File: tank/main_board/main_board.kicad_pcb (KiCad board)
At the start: 2 copper layers, 66.5 x 56.2 mm, 41 parts, among them J1 PowerOut, J10 PowerMotor, J11 SigOut, J12 Spk, J14 M0, J15 M1, J16 M2, J2 PowerIn, J3 Encoder0, J4 Encoder1, J5 Encoder2, J6 Encoder3, J7 Bump0, J8 Bump1, J9 Programming Header, U1 L7805, U4 L293D, U5 L293D, Y1 Crystal

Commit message: fixes
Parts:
- removed SN74HC595: SN74HC595, custom:DIP-16_W7.62mm
- added U3: SN74HC595, custom:DIP-16_W7.62mm, F.Cu at (133.6, 103.2)
- renumbered LEDs to J13, ATMEGA328P-PU to U2

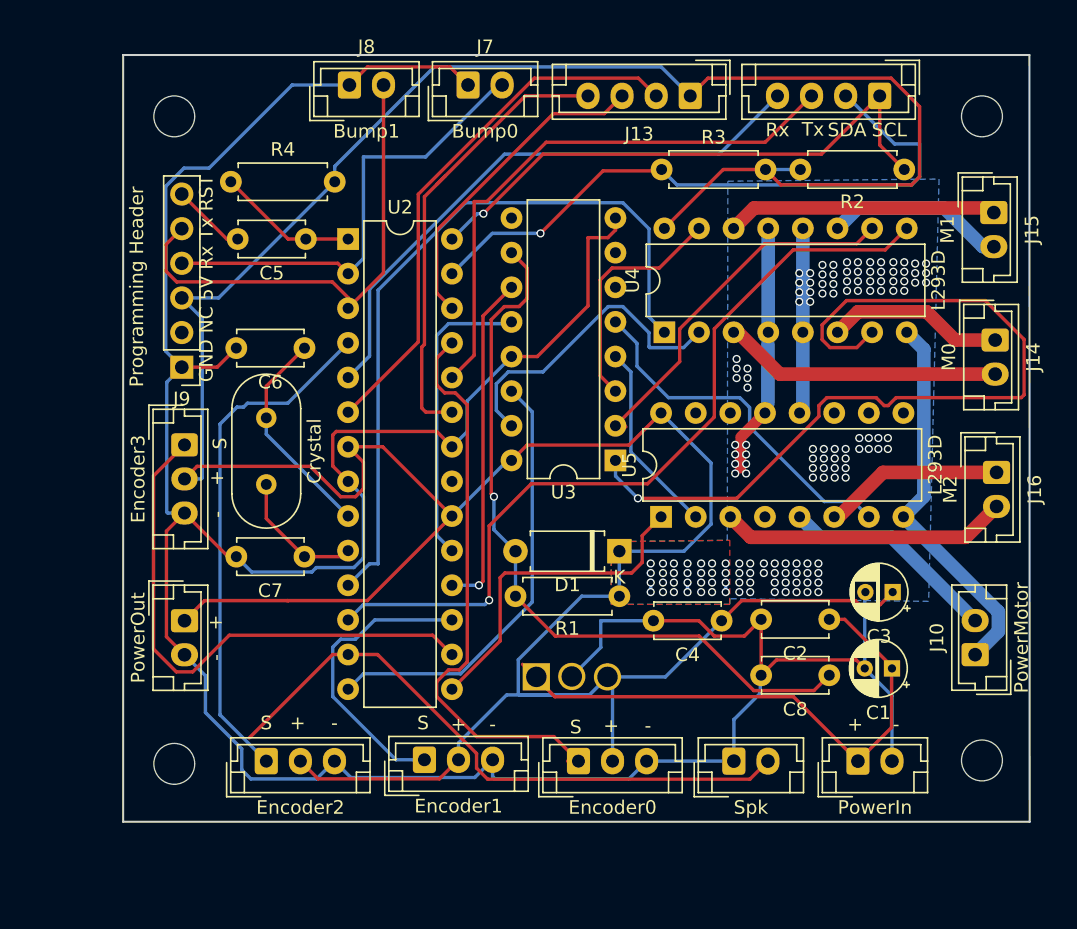
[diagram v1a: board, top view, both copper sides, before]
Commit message: Version 0.11: - Better labelling - Put LED output on Rx and Tx pins. This way, we won't be attaching interrutps to Serial pins
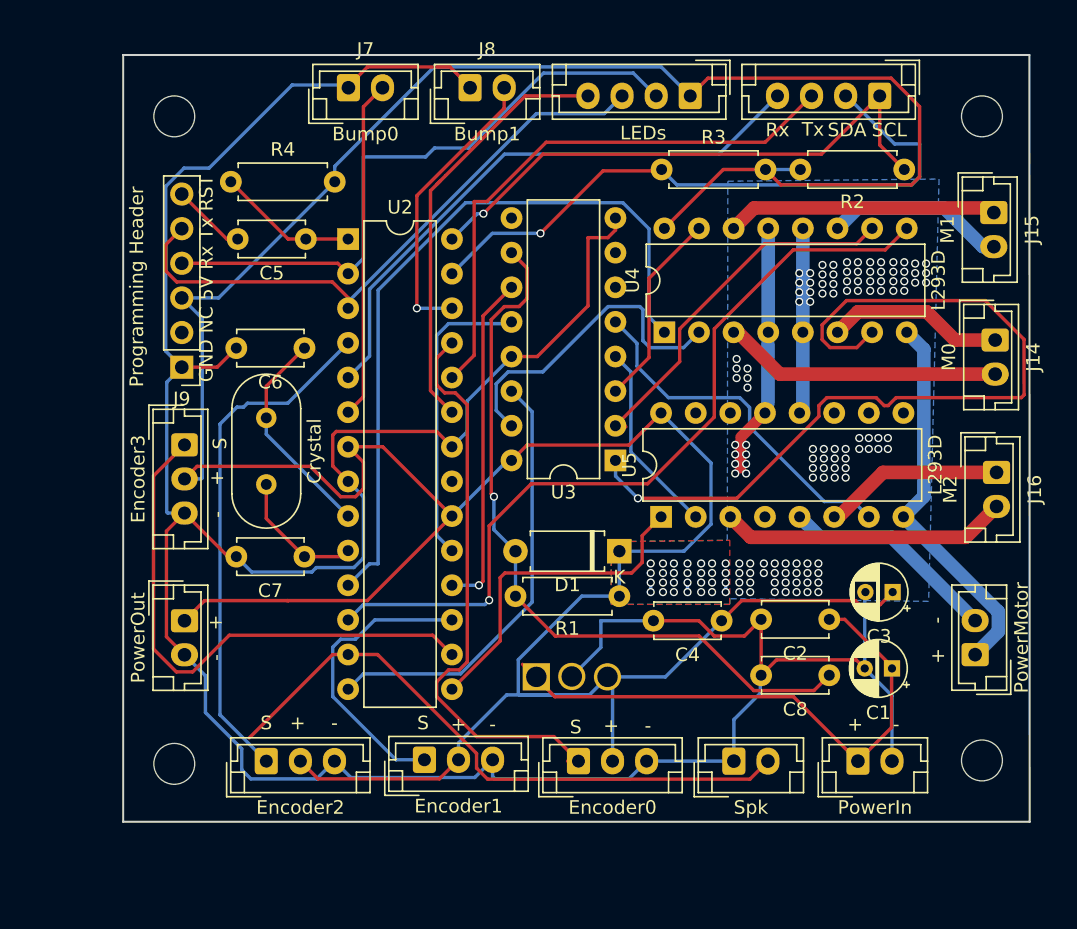
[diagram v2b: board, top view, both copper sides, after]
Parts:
- moved J8 8.85 mm to (123.0, 75.9)
- moved J7 8.78 mm to (114.0, 75.9)
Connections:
- J9 pad 4: Bump0 -> LED0
- J9 pad 5: Bump1 -> LED1
- U2 pad 2: Bump0 -> LED0
- U2 pad 26: LED1 -> Bump1
- U2 pad 3: Bump1 -> LED1
- U2 pad 6: LED0 -> Bump0
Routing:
- net LED1: track 23.9 -> 45.4 mm
- net Bump1: track 36.0 -> 21.7 mm, vias 0 -> 1
- net Bump0: track 33.9 -> 24.8 mm
- net LED0: track 39.6 -> 46.3 mm
- net M1-: track 17.4 -> 14.5 mm
- net LED2: track 33.9 -> 31.7 mm
- net M0+: track 23.4 -> 24.2 mm
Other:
- board text added: "Laser Tag Robot Tank Main Board v0.11 M.I.A.R. Labs nick.groesz@gmail.com"
- board text removed: "Laser Tag Robot Tank Main Board v1.00 M.I.A.R. Labs nick.groesz@gmail.com"

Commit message: debug
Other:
- net class Default removed
- net class Motor removed

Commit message: Main Board v0.12
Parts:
- removed ?: , 
- removed D1: D, custom:D_A-405_P7.62mm_Horizontal
- removed R4: R10, custom:R_Axial_DIN0207_L6.3mm_D2.5mm_P7.62mm_Horizontal
- removed the REF** at (160.5, 125.2)
- removed the REF** at (160.5, 78.0)
- removed the REF** at (101.2, 125.5)
- removed the REF** at (101.2, 78.0)
- added C9: 100nF, custom:C_Disc_D4.7mm_W2.5mm_P5.00mm, F.Cu at (149.0, 104.5)
- added REF**: MountingHole_3mm, custom:MountingHole_3mm, F.Cu at (94.5, 76.5)
- added REF**: MountingHole_3mm, custom:MountingHole_3mm, F.Cu at (159.0, 76.5)
- added REF**: MountingHole_3mm, custom:MountingHole_3mm, F.Cu at (94.0, 130.5)
- added REF**: MountingHole_3mm, custom:MountingHole_3mm, F.Cu at (159.0, 131.0)
- C1: value CP1 -> 10uF
- C2: value C2 -> 100nF
- C3: value CP3 -> 10uF
- C4: value C4 -> 100nF
- C5, C8: value C_Small -> 100nF
- C6: value C6 -> 22pF
- C7: value C7 -> 22pF
- J1: value PowerOut -> Encoder0; footprint custom:JST_EH_B2B-EH-A_1x02_P2.50mm_Vertical -> custom:JST_EH_B3B-EH-A_1x03_P2.50mm_Vertical
- J11: value SigOut -> M0; footprint custom:JST_EH_B4B-EH-A_1x04_P2.50mm_Vertical -> custom:JST_EH_B2B-EH-A_1x02_P2.50mm_Vertical
- J12: value Spk -> M1
- J13: value LEDs -> M2; footprint custom:JST_EH_B4B-EH-A_1x04_P2.50mm_Vertical -> custom:JST_EH_B2B-EH-A_1x02_P2.50mm_Vertical
- J14: value M0 -> Spk
- J15: value M1 -> LEDs; footprint custom:JST_EH_B2B-EH-A_1x02_P2.50mm_Vertical -> custom:JST_EH_B4B-EH-A_1x04_P2.50mm_Vertical
- J16: value M2 -> SigOut; footprint custom:JST_EH_B2B-EH-A_1x02_P2.50mm_Vertical -> custom:JST_EH_B4B-EH-A_1x04_P2.50mm_Vertical
- J2: value PowerIn -> Encoder1; footprint custom:JST_EH_B2B-EH-A_1x02_P2.50mm_Vertical -> custom:JST_EH_B3B-EH-A_1x03_P2.50mm_Vertical
- J3: value Encoder0 -> Encoder2
- J4: value Encoder1 -> Encoder3
- J5: value Encoder2 -> Programming Header; footprint custom:JST_EH_B3B-EH-A_1x03_P2.50mm_Vertical -> custom:PinHeader_1x06_P2.54mm_Vertical
- J6: value Encoder3 -> Bump0; footprint custom:JST_EH_B3B-EH-A_1x03_P2.50mm_Vertical -> custom:JST_EH_B2B-EH-A_1x02_P2.50mm_Vertical
- J7: value Bump0 -> Bump1
- J8: value Bump1 -> PowerOut
- J9: value Programming Header -> PowerIn; footprint custom:PinHeader_1x06_P2.54mm_Vertical -> custom:JST_EH_B2B-EH-A_1x02_P2.50mm_Vertical
- R1: value R -> 10k
- R2: value R7 -> 10k
- R3: value R6 -> 10k
- U1: footprint Custom:L7805CV -> custom:L7805CV
- moved J2 63.5 mm to (95.1, 96.0), turned to -90 degrees
- moved J15 55.5 mm to (129.8, 130.7), turned to 0 degrees
- moved G*** 54.6 mm to (103.6, 81.3)
- moved C2 51.3 mm to (102.5, 94.0), turned to 90 degrees
- moved J13 46.3 mm to (158.5, 118.5), turned to 90 degrees
- moved J16 42.5 mm to (128.5, 77.5), turned to 180 degrees
- moved J14 40.5 mm to (143.5, 130.7), turned to 0 degrees
- moved J3 40.0 mm to (95.1, 107.5), turned to -90 degrees
- moved R1 39.3 mm to (108.8, 83.0)
- moved R2 35.0 mm to (119.8, 83.0)
- moved C4 34.6 mm to (125.0, 84.5), turned to 0 degrees
- moved J9 34.1 mm to (100.5, 130.5), turned to 0 degrees
- moved C1 33.8 mm to (120.5, 123.8), turned to 0 degrees
- moved C3 33.7 mm to (120.6, 117.9), turned to 0 degrees
- moved J1 31.3 mm to (95.1, 84.5)
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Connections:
- C2 pad 1: 9V -> 4.5V
- C8 pad 1: Net-(C8-Pad1) -> GND
- C8 pad 2: GND -> 4.5V
- J1 pad 1: 4.5V -> Encoder0
- J1 pad 2: GND -> 4.5V
- J10 pad 2: Gm -> GND
- J11 pad 1: SCL -> Net-(J11-Pad1)
- J11 pad 2: SDA -> Net-(J11-Pad2)
- J12 pad 1: GND -> Net-(J12-Pad1)
- J12 pad 2: SPK -> Net-(J12-Pad2)
- J13 pad 1: 4.5V -> Net-(J13-Pad1)
- J13 pad 2: LED0 -> Net-(J13-Pad2)
- J14 pad 1: Net-(J14-Pad1) -> GND
- J14 pad 2: Net-(J14-Pad2) -> SPK
- J15 pad 1: Net-(J15-Pad1) -> 4.5V
- J15 pad 2: Net-(J15-Pad2) -> LED0
- J16 pad 1: Net-(J16-Pad1) -> SCL
- J16 pad 2: Net-(J16-Pad2) -> SDA
- J2 pad 1: 9V -> Encoder1
- J2 pad 2: GND -> 4.5V
- J3 pad 1: Encoder0 -> Encoder2
- J4 pad 1: Encoder1 -> Encoder3
- J5 pad 1: Encoder2 -> GND
- J5 pad 2: 4.5V -> unconnected-(J5-Pad2)
- J5 pad 3: GND -> 4.5V
- J6 pad 1: Encoder3 -> GND
- J6 pad 2: 4.5V -> Bump0
- J7 pad 2: Bump0 -> Bump1
- J8 pad 1: GND -> 4.5V
- J8 pad 2: Bump1 -> GND
- J9 pad 1: GND -> 9V
- J9 pad 2: Net-(J9-Pad2) -> GND
- R1 pad 1: 4.5V -> SCL
- R1 pad 2: Net-(C8-Pad1) -> 4.5V
- R2 pad 1: SCL -> SDA
- R3 pad 1: SDA -> Net-(C5-Pad1)
- U2 pad 21: Net-(U2-Pad21) -> unconnected-(U2-Pad21)
- U3 pad 10: Net-(C8-Pad1) -> 4.5V
- U3 pad 6: Net-(U3-Pad6) -> unconnected-(U3-Pad6)
- U3 pad 7: Net-(U3-Pad7) -> unconnected-(U3-Pad7)
- U3 pad 9: Net-(U3-Pad9) -> unconnected-(U3-Pad9)
- U4 pad 11: Net-(J15-Pad2) -> Net-(J12-Pad2)
- U4 pad 12: Gm -> GND
- U4 pad 13: Gm -> GND
- U4 pad 14: Net-(J15-Pad1) -> Net-(J12-Pad1)
- U4 pad 3: Net-(J14-Pad2) -> Net-(J11-Pad2)
- U4 pad 4: Gm -> GND
- U4 pad 5: Gm -> GND
- U4 pad 6: Net-(J14-Pad1) -> Net-(J11-Pad1)
- U5 pad 10: Net-(U5-Pad10) -> unconnected-(U5-Pad10)
- U5 pad 11: Net-(U5-Pad11) -> unconnected-(U5-Pad11)
- U5 pad 12: Gm -> GND
- U5 pad 13: Gm -> GND
- U5 pad 14: Net-(U5-Pad14) -> unconnected-(U5-Pad14)
- U5 pad 15: Net-(U5-Pad15) -> unconnected-(U5-Pad15)
- U5 pad 3: Net-(J16-Pad2) -> Net-(J13-Pad2)
- U5 pad 4: Gm -> GND
- U5 pad 5: Gm -> GND
- U5 pad 6: Net-(J16-Pad1) -> Net-(J13-Pad1)
- U5 pad 9: Net-(U5-Pad9) -> unconnected-(U5-Pad9)
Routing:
- net GND: track 228.1 -> 334.4 mm, vias 0 -> 186
- net M1-: track 14.5 -> 79.2 mm
- net Net-(C8-Pad1): track 54.5 -> 0.00 mm, vias 1 -> 0
- net M0PWM: track 54.3 -> 105.4 mm, vias 0 -> 1
- net Vm: track 28.4 -> 77.9 mm
- net Gm: track 48.4 -> 0.00 mm, vias 142 -> 0
- net 4.5V: track 272.2 -> 319.9 mm, vias 0 -> 1
- net M0-: track 62.1 -> 18.0 mm, vias 1 -> 0
- net M1PWM: track 59.9 -> 99.2 mm
- net M2PWM: track 24.4 -> 63.7 mm, vias 0 -> 1
- net M0+: track 24.2 -> 62.5 mm
- net Net-(C5-Pad2): track 5.47 -> 34.7 mm, vias 0 -> 1
- net SERIAL_DATA: track 32.3 -> 58.9 mm, vias 0 -> 1
- net M2+: track 14.2 -> 36.9 mm
- net Net-(J16-Pad2): track 21.1 -> 0.00 mm
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- added copper zone on B.Cu, net GND
- added copper zone on F.Cu, net GND
- removed copper zone on B.Cu, net Gm
- removed copper zone on F.Cu, net Gm
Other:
- board size 66.5 x 56.2 mm -> 71.5 x 61.5 mm
- board text added: "Main Board v0.12 Laser Tag Robot Tank M.I.A.R. Labs nick.groesz@gmail.com"
- board text removed: "+"
- board text removed: "-"
- board text removed: "GND NC 5V Rx Tx RST"
- board text removed: "Laser Tag Robot Tank Main Board v0.11 M.I.A.R. Labs nick.groesz@gmail.com"
- board text removed: "Rx"
- board text removed: "S"
- board text removed: "SCL"
- board text removed: "SDA"
- board text removed: "Tx"

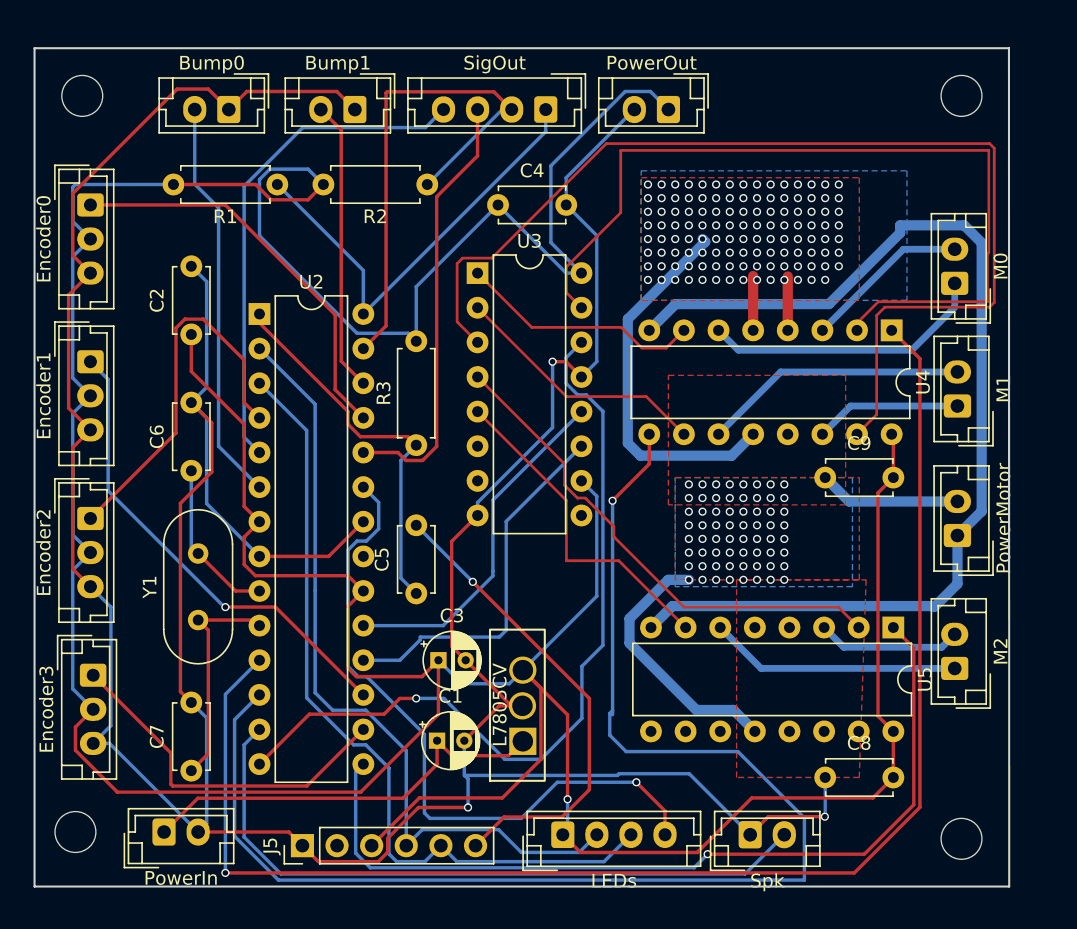
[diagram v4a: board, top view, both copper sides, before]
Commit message: modifying main board still need to finish PCB layout updates:     - speaker gets resistor     - net tie between logical ground and motor ground
i would like to flip the motor ICs and add some more space
around motor ICs and also a little more space around some of
the JST connectors
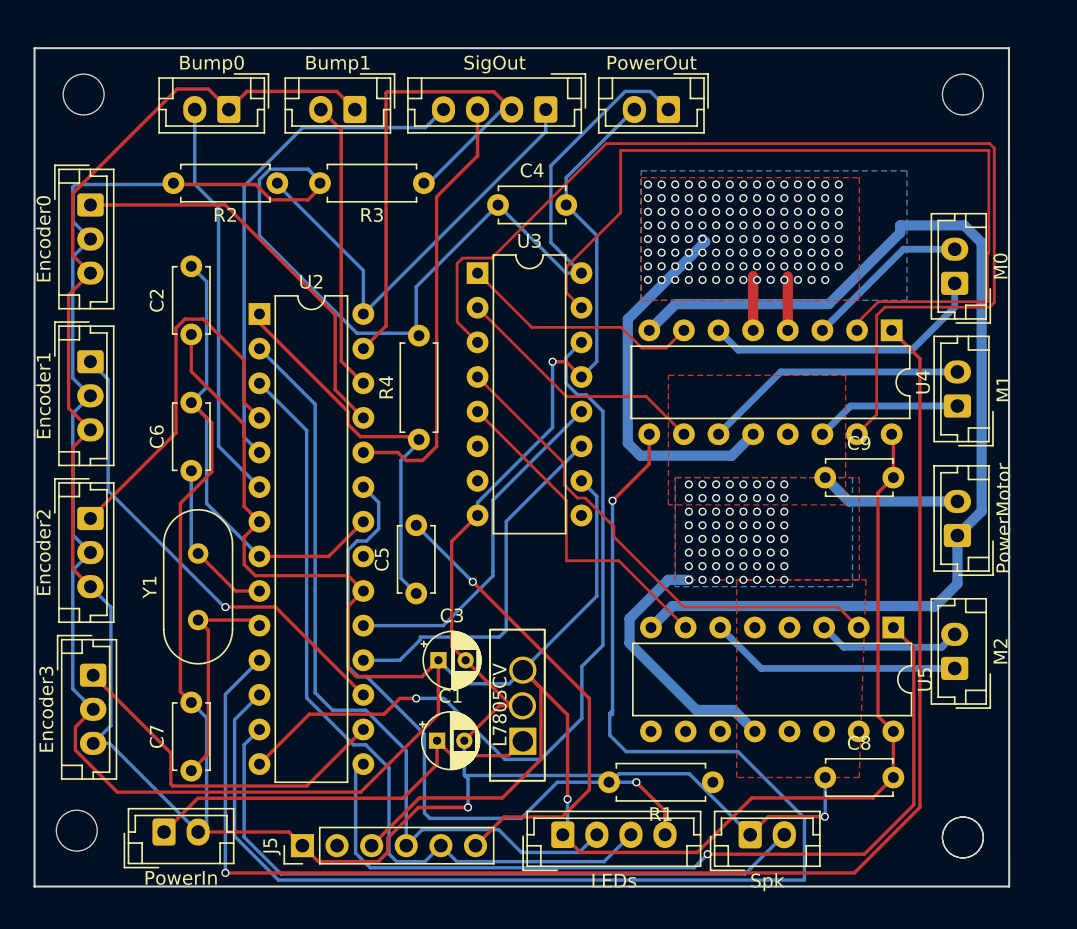
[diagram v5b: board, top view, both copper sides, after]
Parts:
- removed G***: LOGO, custom:Tank
- removed the REF** at (94.5, 76.5)
- removed the REF** at (159.0, 76.5)
- removed the REF** at (94.0, 130.5)
- removed the REF** at (159.0, 131.0)
- added ?: , , F.Cu at (159.1, 130.9)
- added R4: 10k, custom:R_Axial_DIN0207_L6.3mm_D2.5mm_P7.62mm_Horizontal, F.Cu at (119.2, 101.7)
- added REF**: MountingHole_3mm, custom:MountingHole_3mm, F.Cu at (94.6, 76.4)
- added REF**: MountingHole_3mm, custom:MountingHole_3mm, F.Cu at (159.1, 130.9)
- added REF**: MountingHole_3mm, custom:MountingHole_3mm, F.Cu at (159.1, 76.4)
- added REF**: MountingHole_3mm, custom:MountingHole_3mm, F.Cu at (94.1, 130.4)
- moved R1 54.3 mm to (140.8, 126.8)
- moved R3 19.2 mm to (119.6, 82.9), turned to 180 degrees
- moved R2 11.0 mm to (108.8, 82.9)
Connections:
- C8 pad 1: GND -> Gm
- C9 pad 1: GND -> Gm
- J10 pad 2: GND -> Gm
- R1 pad 1: SCL -> (no net)
- R1 pad 2: 4.5V -> (no net)
- R2 pad 1: SDA -> (no net)
- R2 pad 2: 4.5V -> (no net)
- R3 pad 1: Net-(C5-Pad1) -> (no net)
- R3 pad 2: 4.5V -> (no net)
- U2 pad 13: SPK -> Net-(R1-Pad1)
- U4 pad 12: GND -> Gm
- U4 pad 13: GND -> Gm
- U4 pad 4: GND -> Gm
- U4 pad 5: GND -> Gm
- U5 pad 12: GND -> Gm
- U5 pad 13: GND -> Gm
- U5 pad 4: GND -> Gm
- U5 pad 5: GND -> Gm
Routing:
- net Gm: track 0.00 -> 65.2 mm, vias 0 -> 183
- net GND: track 334.4 -> 269.2 mm, vias 186 -> 3
- added copper zone on B.Cu, net Gm
- added copper zone on F.Cu, net Gm
- removed copper zone on B.Cu, net GND
- removed copper zone on F.Cu, net GND
